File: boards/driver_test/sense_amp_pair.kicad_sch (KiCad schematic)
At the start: 15 parts, among them T1 1:1, T2 1:1, U8 SN7524

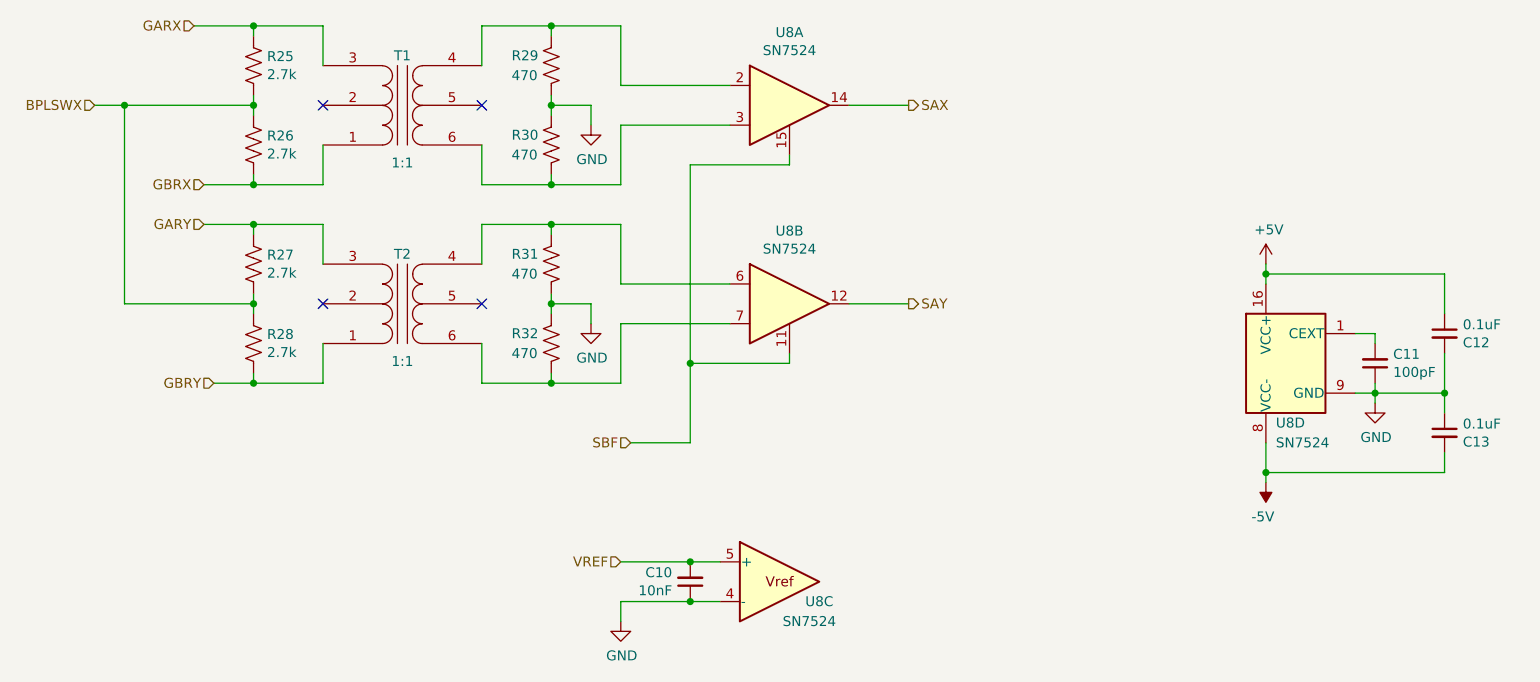
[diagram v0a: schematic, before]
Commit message: Driver test: finished up board layout
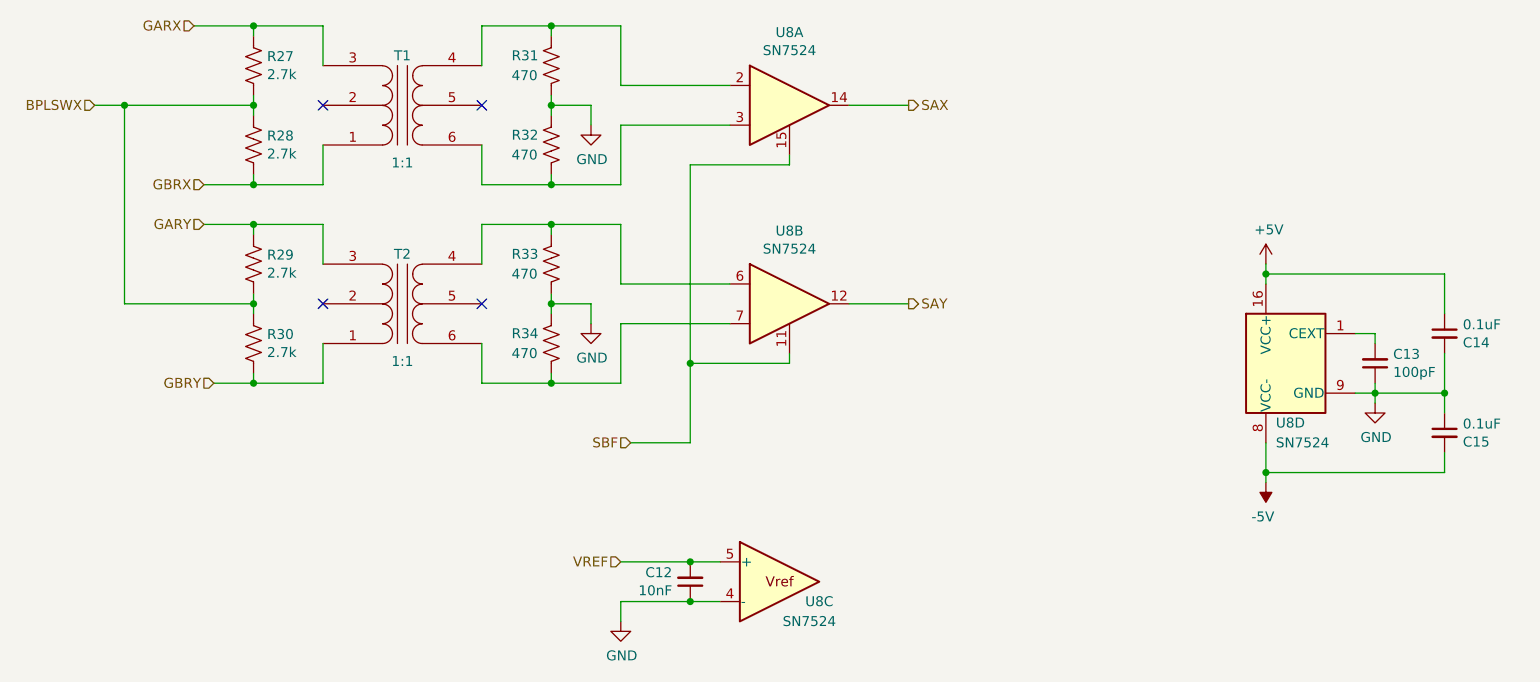
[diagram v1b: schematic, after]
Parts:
- renumbered C10 to C12, C11 to C13, C12 to C14, C13 to C15, R25 to R27, R26 to R28, R27 to R29, R28 to R30, R29 to R31, R30 to R32, R31 to R33, R32 to R34
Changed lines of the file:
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@@
   (symbol (lib_id "Device:R_US") (at 73.66 46.99 0) (unit 1)
     (in_bom yes) (on_board yes)
-    (property "Reference" "R25" (id 0) (at 75.3872 45.8216 0)
+    (property "Reference" "R27" (id 0) (at 75.3872 45.8216 0)
       (effects (font (size 1.27 1.27)) (justify left))
     )
@@
   (symbol (lib_id "Device:R_US") (at 73.66 57.15 0) (unit 1)
     (in_bom yes) (on_board yes)
-    (property "Reference" "R26" (id 0) (at 75.3872 55.9816 0)
+    (property "Reference" "R28" (id 0) (at 75.3872 55.9816 0)
       (effects (font (size 1.27 1.27)) (justify left))
     )
@@
   (symbol (lib_id "Device:R_US") (at 111.76 46.99 0) (mirror y) (unit 1)
     (in_bom yes) (on_board yes)
-    (property "Reference" "R29" (id 0) (at 106.68 45.72 0)
+    (property "Reference" "R31" (id 0) (at 106.68 45.72 0)
       (effects (font (size 1.27 1.27)) (justify right))
     )
@@
   (symbol (lib_id "Device:R_US") (at 111.76 57.15 0) (mirror y) (unit 1)
     (in_bom yes) (on_board yes)
-    (property "Reference" "R30" (id 0) (at 106.68 55.88 0)
+    (property "Reference" "R32" (id 0) (at 106.68 55.88 0)
       (effects (font (size 1.27 1.27)) (justify right))
     )
@@
   (symbol (lib_id "power:GND") (at 116.84 54.61 0) (unit 1)
     (in_bom yes) (on_board yes)
-    (property "Reference" "#PWR036" (id 0) (at 116.84 60.96 0)
+    (property "Reference" "#PWR040" (id 0) (at 116.84 60.96 0)
       (effects (font (size 1.27 1.27)) hide)
     )
@@
   (symbol (lib_id "Device:R_US") (at 73.66 72.39 0) (unit 1)
     (in_bom yes) (on_board yes)
-    (property "Reference" "R27" (id 0) (at 75.3872 71.2216 0)
+    (property "Reference" "R29" (id 0) (at 75.3872 71.2216 0)
       (effects (font (size 1.27 1.27)) (justify left))
     )
@@
   (symbol (lib_id "Device:R_US") (at 73.66 82.55 0) (unit 1)
     (in_bom yes) (on_board yes)
-    (property "Reference" "R28" (id 0) (at 75.3872 81.3816 0)
+    (property "Reference" "R30" (id 0) (at 75.3872 81.3816 0)
       (effects (font (size 1.27 1.27)) (justify left))
     )
@@
   (symbol (lib_id "Device:R_US") (at 111.76 72.39 0) (mirror y) (unit 1)
     (in_bom yes) (on_board yes)
-    (property "Reference" "R31" (id 0) (at 106.68 71.12 0)
+    (property "Reference" "R33" (id 0) (at 106.68 71.12 0)
       (effects (font (size 1.27 1.27)) (justify right))
     )
@@
   (symbol (lib_id "Device:R_US") (at 111.76 82.55 0) (mirror y) (unit 1)
     (in_bom yes) (on_board yes)
-    (property "Reference" "R32" (id 0) (at 106.68 81.28 0)
+    (property "Reference" "R34" (id 0) (at 106.68 81.28 0)
       (effects (font (size 1.27 1.27)) (justify right))
     )
@@
   (symbol (lib_id "power:GND") (at 116.84 80.01 0) (unit 1)
     (in_bom yes) (on_board yes)
-    (property "Reference" "#PWR037" (id 0) (at 116.84 86.36 0)
+    (property "Reference" "#PWR041" (id 0) (at 116.84 86.36 0)
       (effects (font (size 1.27 1.27)) hide)
     )
@@
   (symbol (lib_id "power:GND") (at 217.17 90.17 0) (unit 1)
     (in_bom yes) (on_board yes)
-    (property "Reference" "#PWR041" (id 0) (at 217.17 96.52 0)
+    (property "Reference" "#PWR045" (id 0) (at 217.17 96.52 0)
       (effects (font (size 1.27 1.27)) hide)
     )
@@
   (symbol (lib_id "Device:C_Small") (at 217.17 85.09 180) (unit 1)
     (in_bom yes) (on_board yes)
-    (property "Reference" "C11" (id 0) (at 219.4814 83.9216 0)
+    (property "Reference" "C13" (id 0) (at 219.4814 83.9216 0)
       (effects (font (size 1.27 1.27)) (justify right))
     )
@@
   (symbol (lib_id "Device:C_Small") (at 226.06 81.28 0) (mirror y) (unit 1)
     (in_bom yes) (on_board yes)
-    (property "Reference" "C12" (id 0) (at 228.3968 82.4484 0)
+    (property "Reference" "C14" (id 0) (at 228.3968 82.4484 0)
       (effects (font (size 1.27 1.27)) (justify right))
     )
@@
   (symbol (lib_id "Device:C_Small") (at 226.06 93.98 0) (mirror y) (unit 1)
     (in_bom yes) (on_board yes)
-    (property "Reference" "C13" (id 0) (at 228.3968 95.1484 0)
+    (property "Reference" "C15" (id 0) (at 228.3968 95.1484 0)
       (effects (font (size 1.27 1.27)) (justify right))
     )
@@
   (symbol (lib_id "Device:C_Small") (at 129.54 113.03 0) (mirror x) (unit 1)
     (in_bom yes) (on_board yes)
-    (property "Reference" "C10" (id 0) (at 127.2286 111.8616 0)
+    (property "Reference" "C12" (id 0) (at 127.2286 111.8616 0)
       (effects (font (size 1.27 1.27)) (justify right))
     )
@@
   (symbol (lib_id "power:GND") (at 120.65 118.11 0) (unit 1)
     (in_bom yes) (on_board yes)
-    (property "Reference" "#PWR038" (id 0) (at 120.65 124.46 0)
+    (property "Reference" "#PWR042" (id 0) (at 120.65 124.46 0)
       (effects (font (size 1.27 1.27)) hide)
     )
@@
   (symbol (lib_id "power:+5V") (at 203.2 72.39 0) (unit 1)
     (in_bom yes) (on_board yes)
-    (property "Reference" "#PWR039" (id 0) (at 203.2 76.2 0)
+    (property "Reference" "#PWR043" (id 0) (at 203.2 76.2 0)
       (effects (font (size 1.27 1.27)) hide)
     )
@@
   (symbol (lib_id "power:-5V") (at 203.2 100.33 180) (unit 1)
     (in_bom yes) (on_board yes)
-    (property "Reference" "#PWR040" (id 0) (at 203.2 102.87 0)
-      (effects (font (size 1.27 1.27)) hide)
-    )
+    (property "Reference" "#PWR044" (id 0) (at 203.2 102.87 0)
+      (effects (font (size 1.27 1.27)) hide)
+    )

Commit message: Driver test: some updates to component values based on new documentation
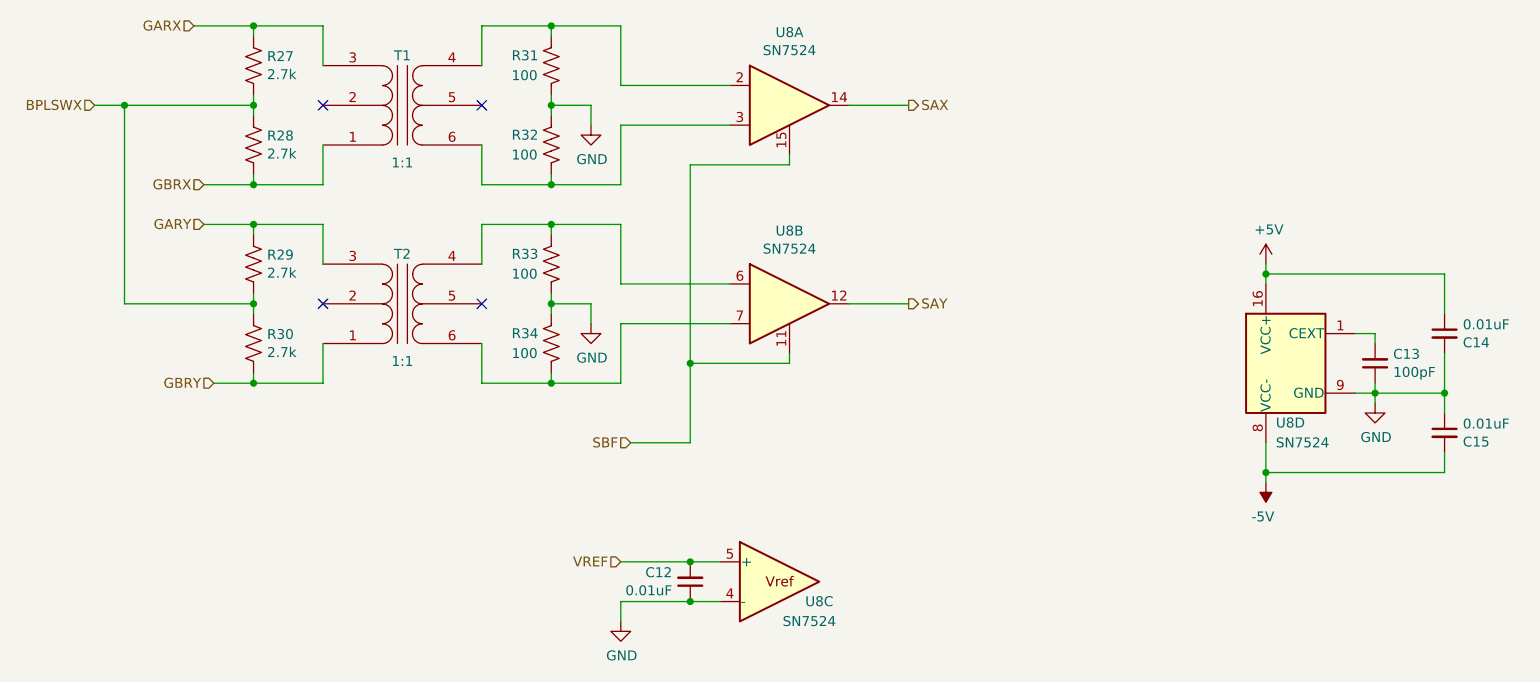
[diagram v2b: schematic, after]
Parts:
- C12: value 10nF -> 0.01uF
- C14, C15: value 0.1uF -> 0.01uF; Rating (none) -> 100V; Tolerance (none) -> 10%
- R31, R32, R33, R34: value 470 -> 100
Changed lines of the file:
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@@
       (effects (font (size 1.27 1.27)) (justify right))
     )
-    (property "Value" "470" (id 1) (at 106.68 48.26 0)
+    (property "Value" "100" (id 1) (at 106.68 48.26 0)
       (effects (font (size 1.27 1.27)) (justify right))
     )
@@
       (effects (font (size 1.27 1.27)) (justify right))
     )
-    (property "Value" "470" (id 1) (at 106.68 58.42 0)
+    (property "Value" "100" (id 1) (at 106.68 58.42 0)
       (effects (font (size 1.27 1.27)) (justify right))
     )
@@
       (effects (font (size 1.27 1.27)) (justify right))
     )
-    (property "Value" "470" (id 1) (at 106.68 73.66 0)
+    (property "Value" "100" (id 1) (at 106.68 73.66 0)
       (effects (font (size 1.27 1.27)) (justify right))
     )
@@
       (effects (font (size 1.27 1.27)) (justify right))
     )
-    (property "Value" "470" (id 1) (at 106.68 83.82 0)
+    (property "Value" "100" (id 1) (at 106.68 83.82 0)
       (effects (font (size 1.27 1.27)) (justify right))
     )
@@
       (effects (font (size 1.27 1.27)) (justify right))
     )
-    (property "Value" "0.1uF" (id 1) (at 228.3968 80.137 0)
+    (property "Value" "0.01uF" (id 1) (at 228.3968 80.137 0)
       (effects (font (size 1.27 1.27)) (justify right))
     )
@@
       (effects (font (size 1.27 1.27)) hide)
     )
+    (property "Rating" "100V" (id 4) (at 226.06 81.28 0)
+      (effects (font (size 1.27 1.27)) hide)
+    )
+    (property "Tolerance" "10%" (id 5) (at 226.06 81.28 0)
+      (effects (font (size 1.27 1.27)) hide)
+    )
     (pin "1")
     (pin "2")
@@
       (effects (font (size 1.27 1.27)) (justify right))
     )
-    (property "Value" "0.1uF" (id 1) (at 228.3968 92.837 0)
+    (property "Value" "0.01uF" (id 1) (at 228.3968 92.837 0)
       (effects (font (size 1.27 1.27)) (justify right))
     )
@@
     )
     (property "Datasheet" "~" (id 3) (at 226.06 93.98 0)
+      (effects (font (size 1.27 1.27)) hide)
+    )
+    (property "Rating" "100V" (id 4) (at 226.06 93.98 0)
+      (effects (font (size 1.27 1.27)) hide)
+    )
+    (property "Tolerance" "10%" (id 5) (at 226.06 93.98 0)
       (effects (font (size 1.27 1.27)) hide)
     )
@@
       (effects (font (size 1.27 1.27)) (justify right))
     )
-    (property "Value" "10nF" (id 1) (at 127.2286 114.173 0)
-      (effects (font (size 1.27 1.27)) (justify right))
-    )
+    (property "Value" "0.01uF" (id 1) (at 127.2286 114.173 0)
+      (effects (font (size 1.27 1.27)) (justify right))
+    )
